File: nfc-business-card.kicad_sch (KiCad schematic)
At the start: 8 parts, among them U1 NT3H2111W0FHKH

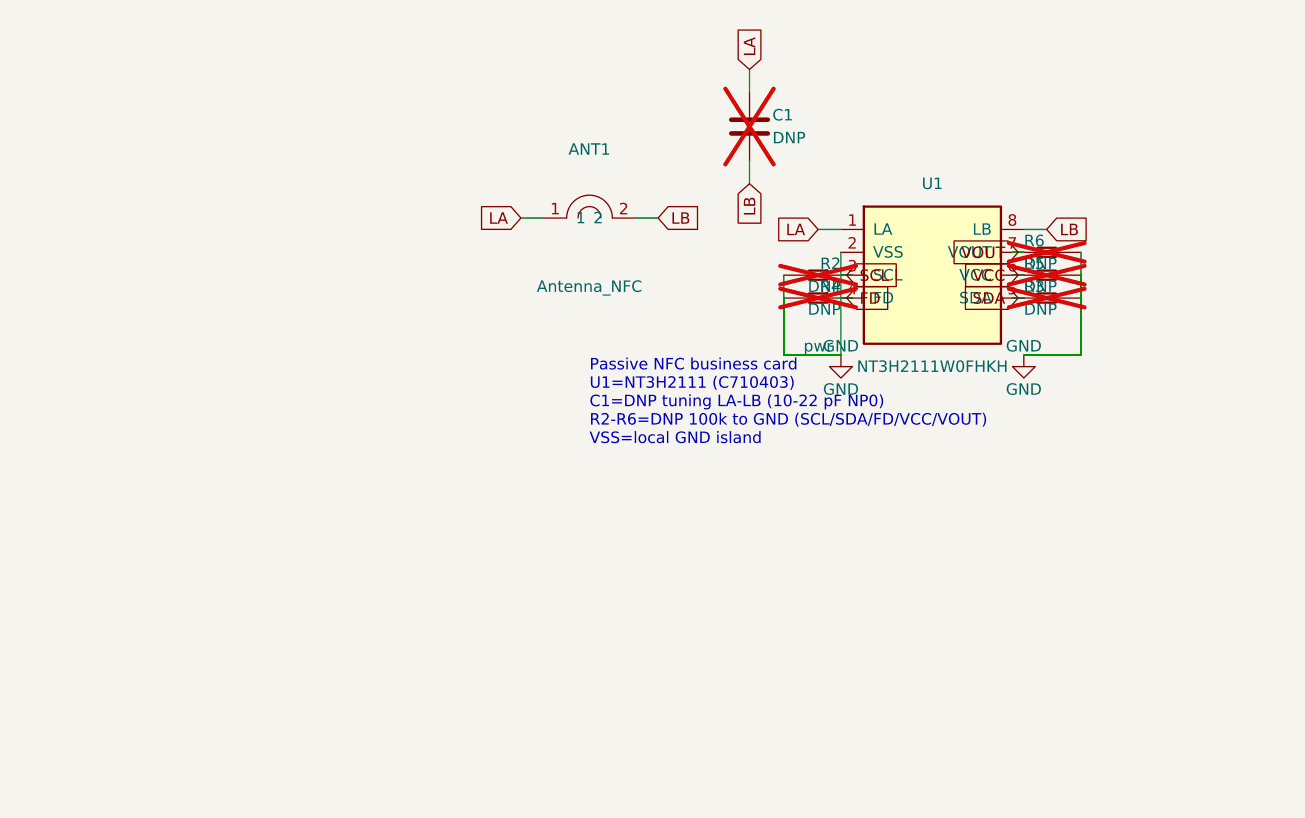
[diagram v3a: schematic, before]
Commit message: refactor: tidy schematic layout with label-joined RF and R bank
Replace spaghetti NC/RF wiring with ANT–C1–U1 labels, a spaced vertical
R2–R6 pull-down row, and a segmented GND rail so ERC and parity stay clean.
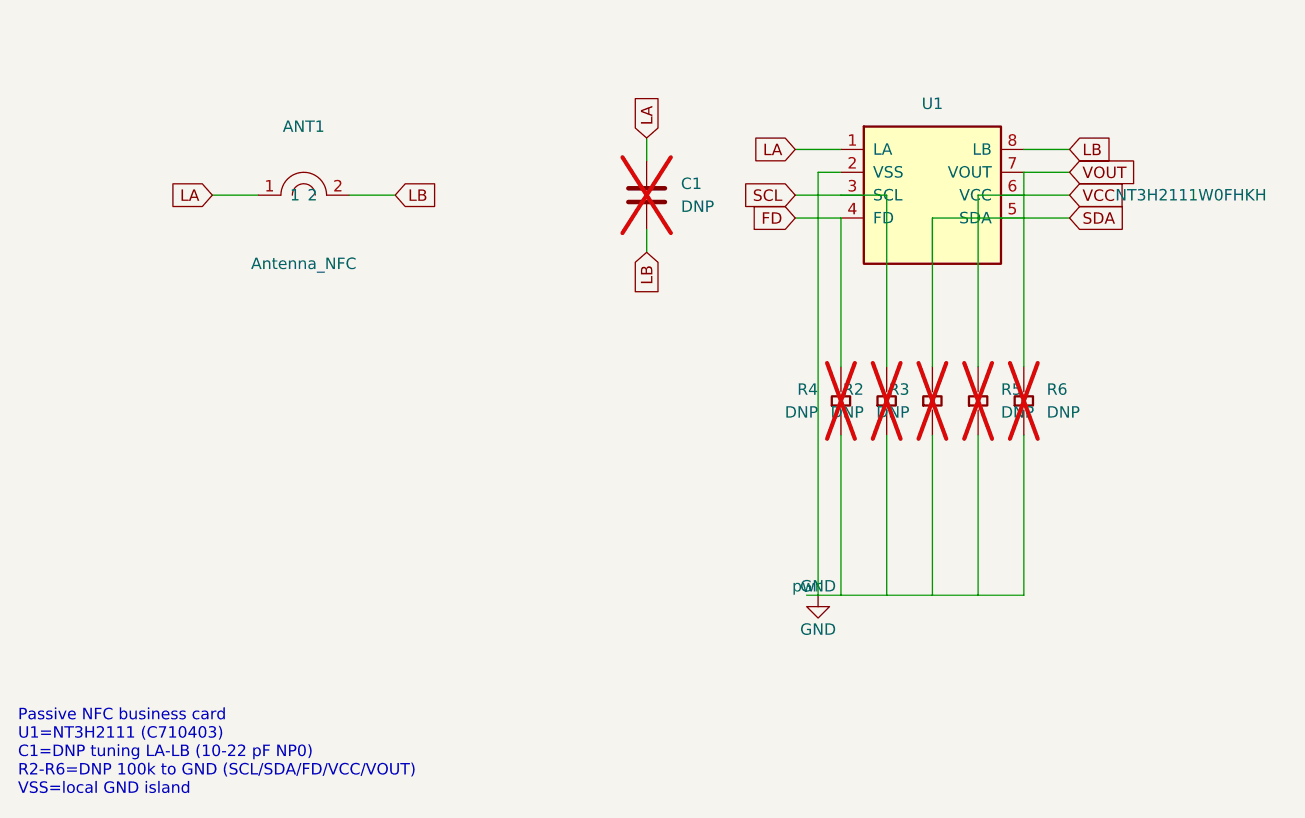
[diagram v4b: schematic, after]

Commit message: refactor: widen LA/LB bus gap and keep schematic R bank off the U1 body
- FEED_BUS_W_MM=0.18 (XQFN ROW) on the 0.40 mm-pitch bus columns:
  parallel pair gap 0.15 -> 0.22 mm, still antenna width elsewhere, no
  width step at the XQFN pads
- schematic R2-R6 columns moved outside the U1 symbol body so no vertical
  or jog crosses the rectangle; net labels on the outward jog/stub
- second GND symbol (#PWR02) on the rail's right end; title-block date
  now generated at write time
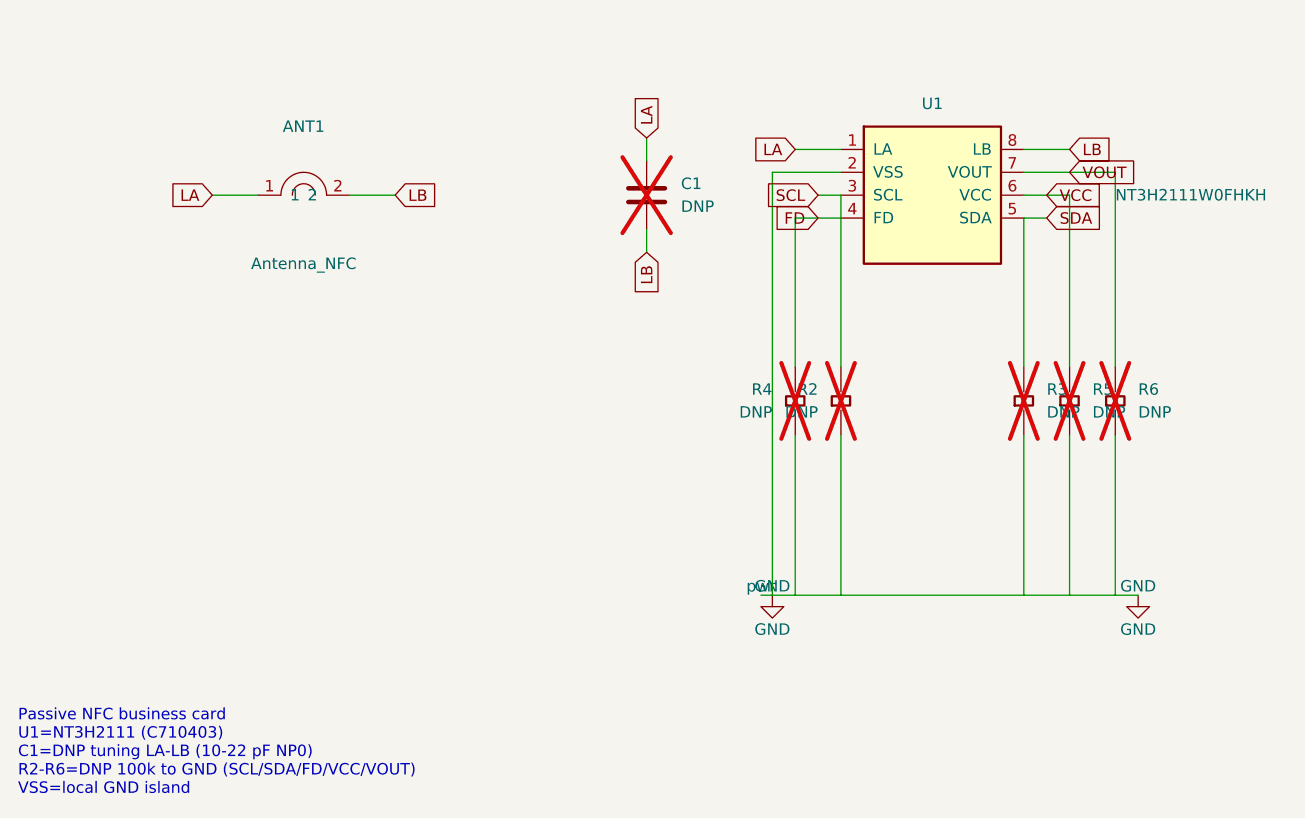
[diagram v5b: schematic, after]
